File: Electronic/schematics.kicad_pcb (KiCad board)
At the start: 2 copper layers, 57.1 x 58 mm, 28 parts, among them J1 Jack-DC, J2 Conn_01x04_Socket, J3 Conn_01x03, U1 ESP32-S3-DEVKITC-1-N16R8V, U2 TMC2209_SILENTSTEPSTICK, U3 DC-DC 12V-5V buck, U4 74HC14

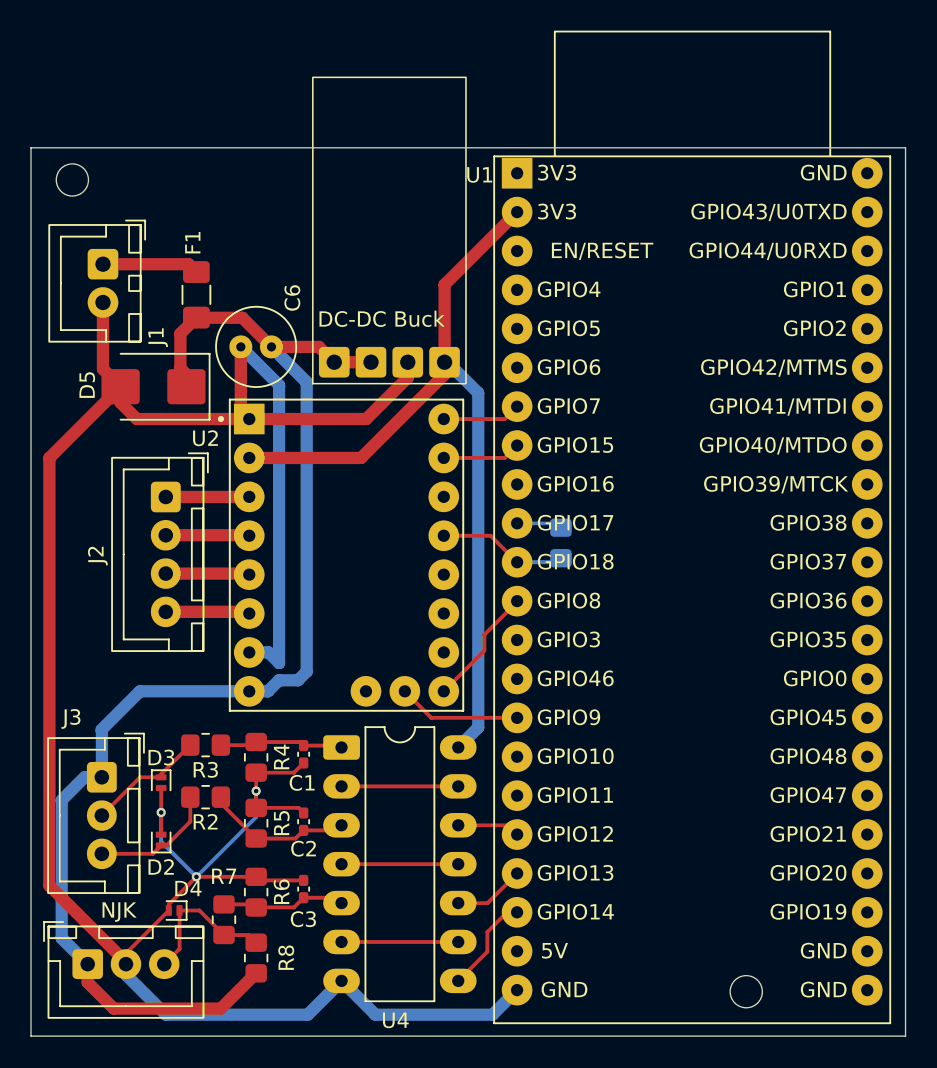
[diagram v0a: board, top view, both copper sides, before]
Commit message: Refactor schematics and update PCB images
- Removed unconnected items from the KiCad project file.
- Removed a diode symbol (PESD3V3S1UL) and its associated properties from the schematic.
- Renamed and repositioned several pins in the TMC2209_SILENTSTEPSTICK symbol for clarity.
- Cleaned up unnecessary junctions and wires in the schematic.
- Updated multiple PCB and schematic images to reflect recent design changes.
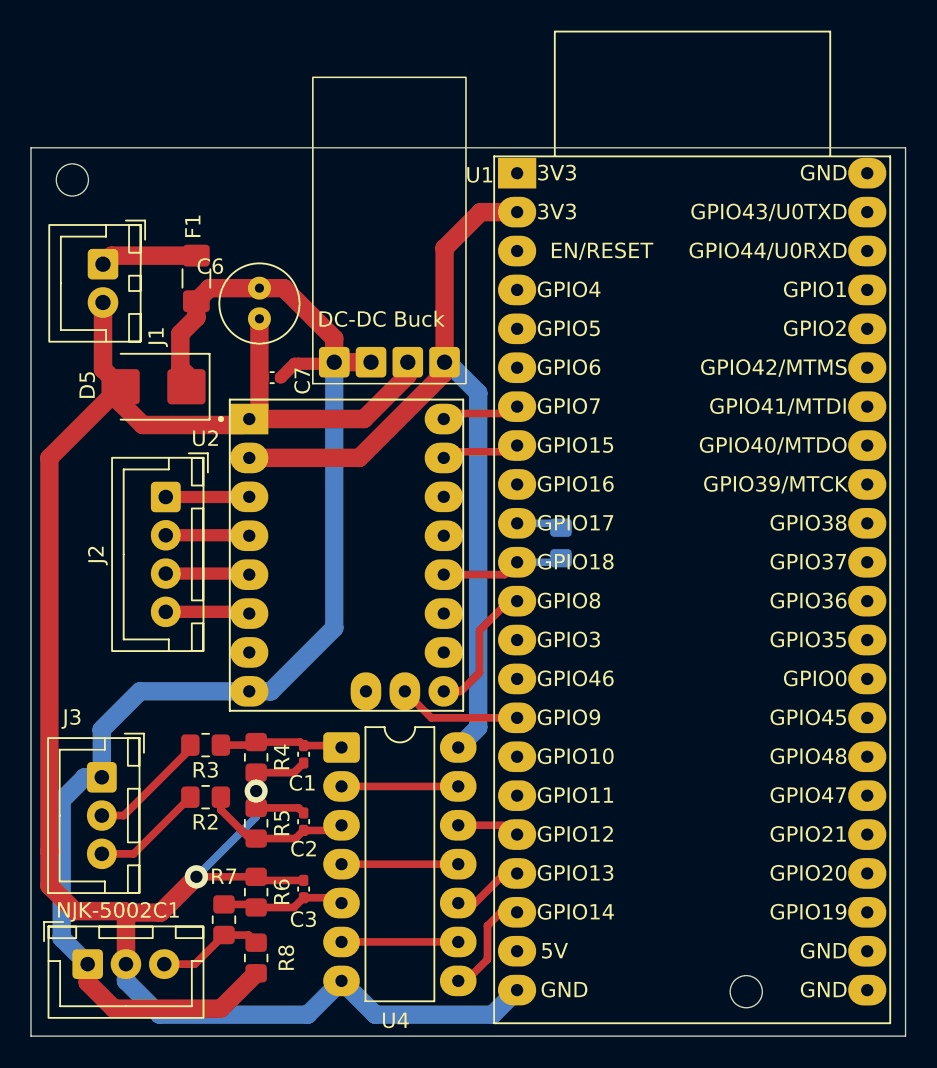
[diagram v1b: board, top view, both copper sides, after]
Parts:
- removed D2, D3, D4: PESD3V3S1UL, Diode_SMD:D_SOD-882
- C6: value 100uF -> 470uF
- C7: moved to F.Cu
- U3: value DC-DC 12V-5V buck -> DC-DC 12V-3V buck
- moved C7 19.2 mm to (133.5, 81.4), turned to 180 degrees
- moved C6 3.91 mm to (132.7, 75.6), turned to -90 degrees
- moved F1 1.07 mm to (128.6, 74.9)
- renumbered NJK to NJK-5002C1
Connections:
- U2 pad 12: Net-(U1-GPIO18) -> unconnected-(U2-SPRD-Pad12)
- U2 pad 13: unconnected-(U2-SPRD-Pad13) -> Net-(U1-GPIO18)
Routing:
- net GND: track 167.7 -> 138.5 mm, vias 3 -> 2
- net Net-(D5-A1): track 86.4 -> 91.6 mm
- net Net-(D4-K): track 9.78 -> 6.99 mm
- net 3V3: track 54.3 -> 55.6 mm
- net Net-(U1-GPIO8): track 7.87 -> 8.84 mm
- net Net-(D2-K): track 8.24 -> 7.31 mm
- net Net-(U1-GPIO14): track 6.45 -> 6.98 mm
